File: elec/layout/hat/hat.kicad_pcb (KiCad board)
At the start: 4 copper layers, 72 parts

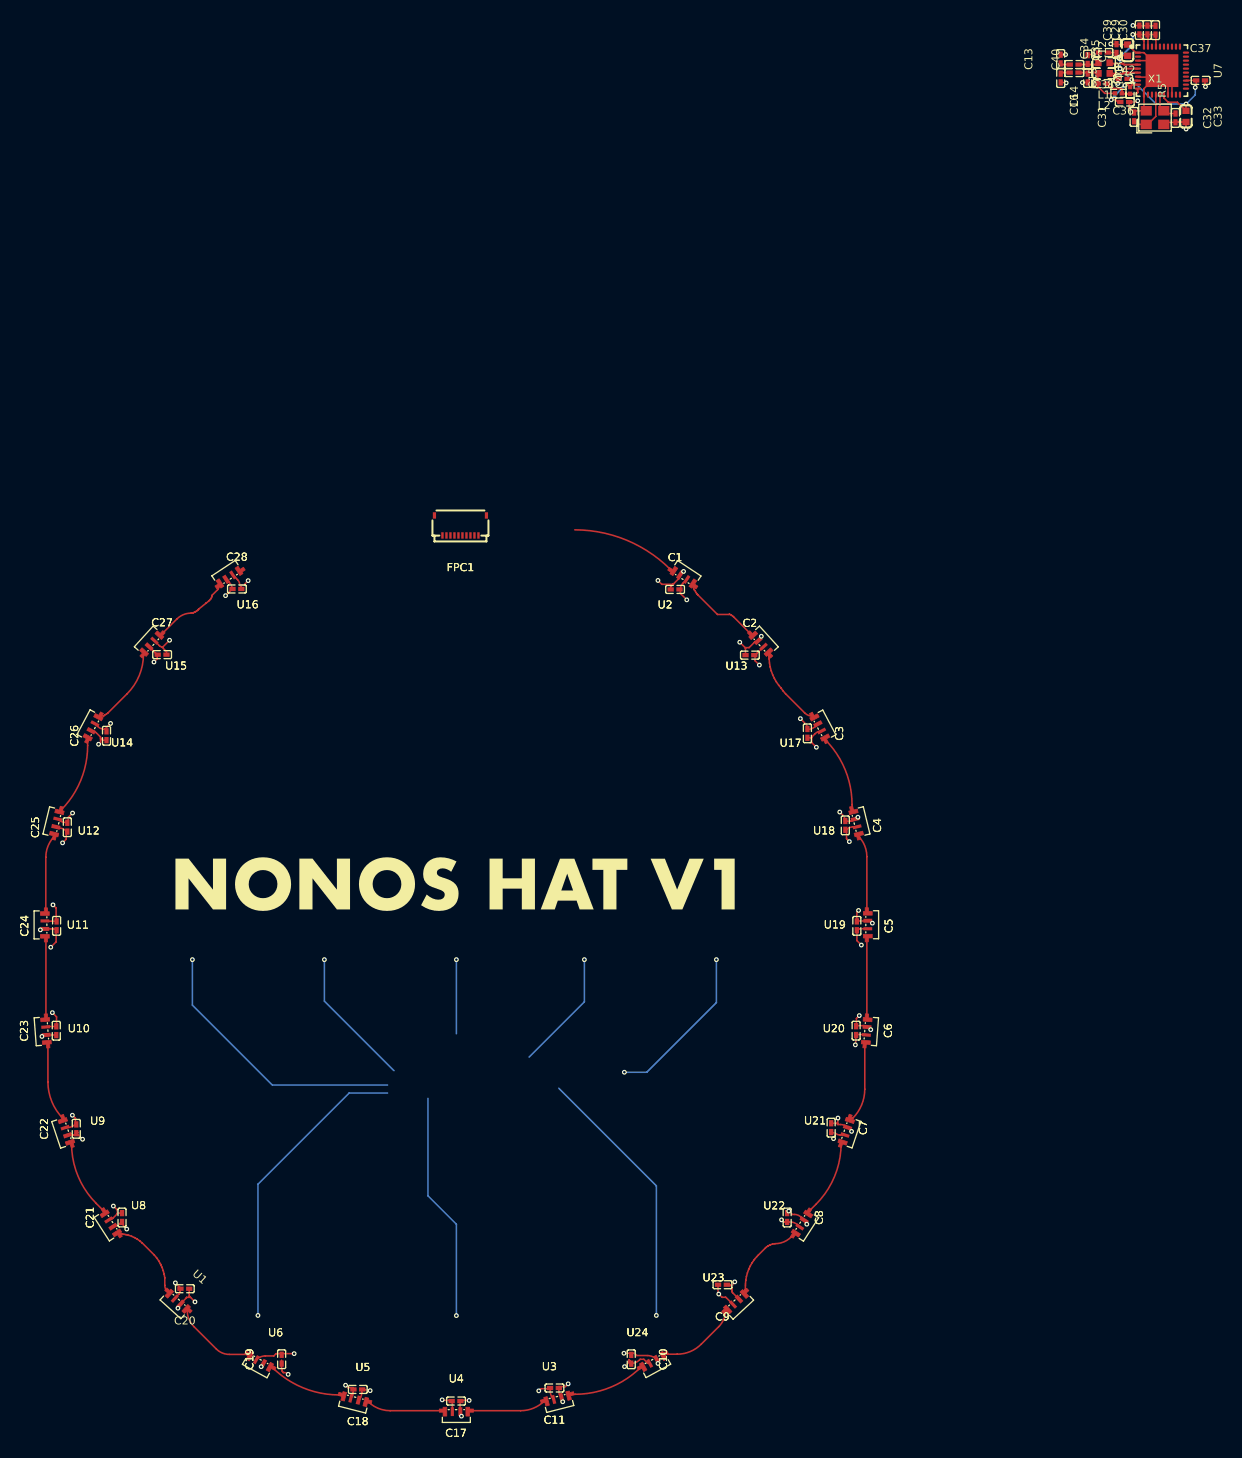
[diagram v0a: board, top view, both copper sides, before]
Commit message: layout updates, level shifter
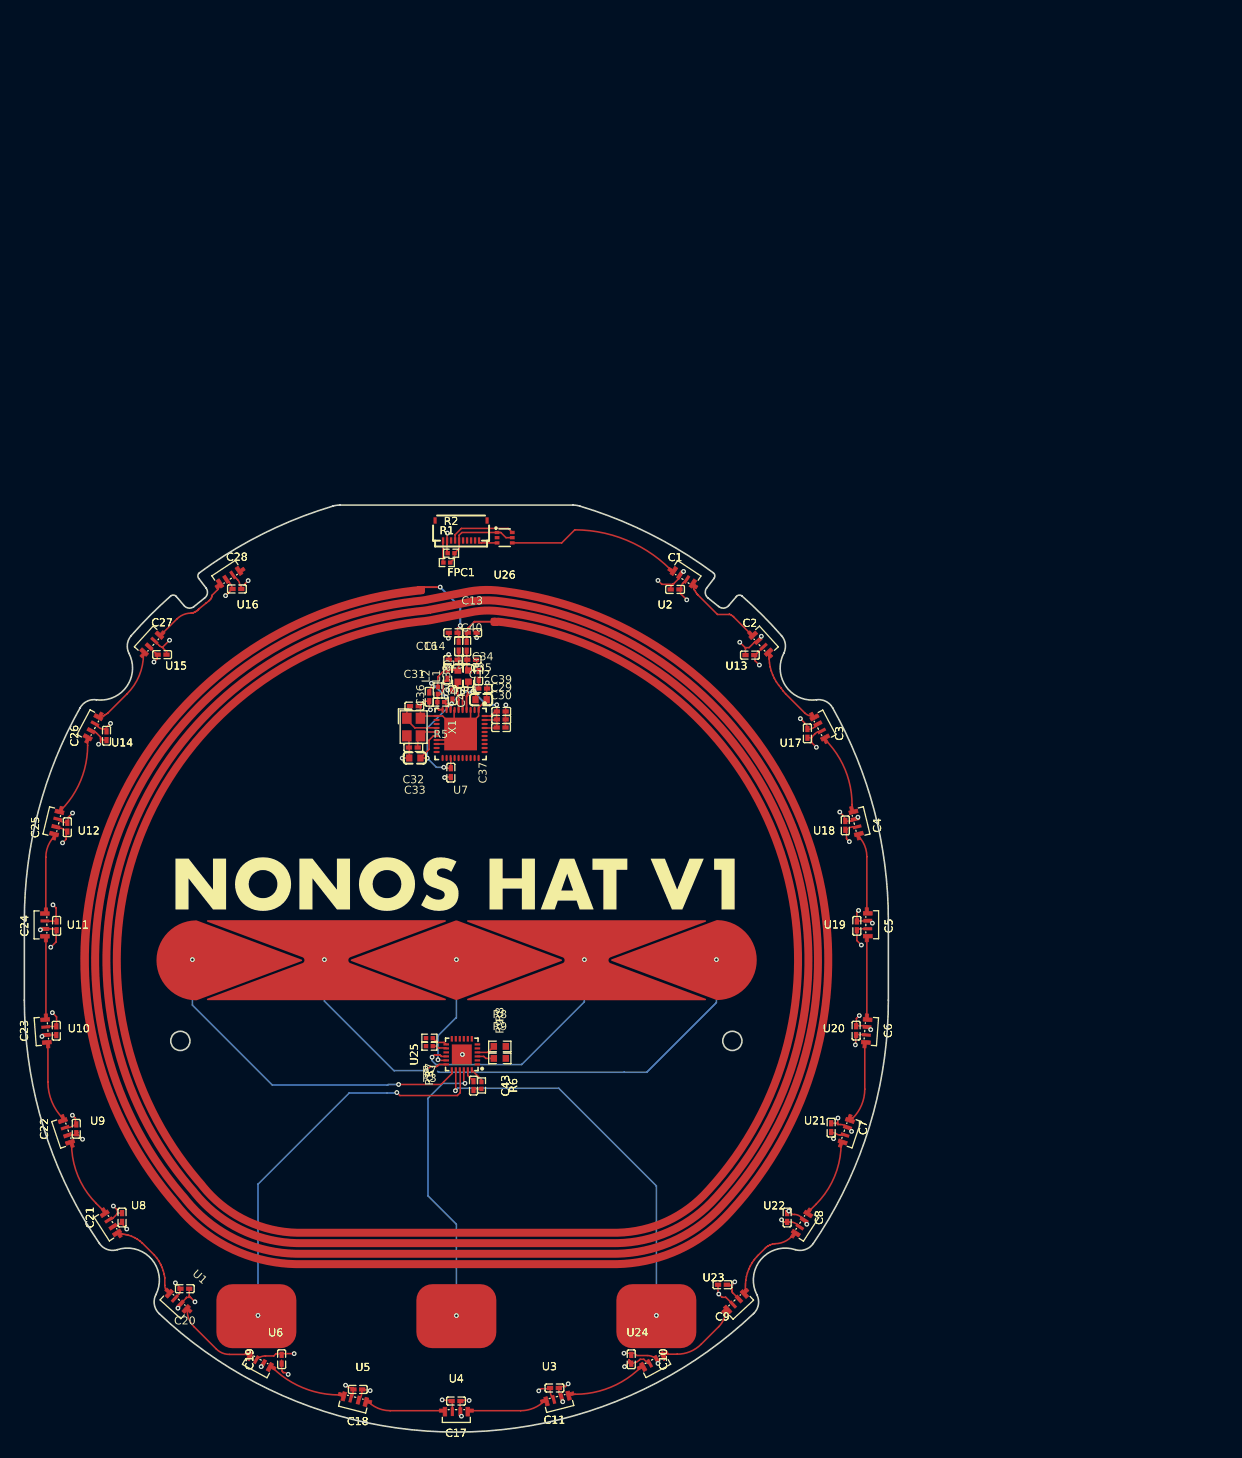
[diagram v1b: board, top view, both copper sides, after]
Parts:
- added ANT1: , hat-button-antenna:hat-button-antenna, F.Cu at (151.8, 91.2)
- added C43: 100nF ±10% 16V X7R, Samsung_Electro_Mechanics_CL05B104KO5NNNC:C0402, F.Cu at (153.9, 106.9)
- added R1: 10kΩ ±1% 62.5mW, UNI_ROYAL_0402WGF1002TCE:R0402, F.Cu at (150.6, 41.5)
- added R2: 10kΩ ±1% 62.5mW, UNI_ROYAL_0402WGF1002TCE:R0402, F.Cu at (151.1, 40.3)
- added R3: 10kΩ ±1% 62.5mW, UNI_ROYAL_0402WGF1002TCE:R0402, F.Cu at (148.4, 101.9)
- added R6: 10kΩ ±1% 62.5mW, UNI_ROYAL_0402WGF1002TCE:R0402, F.Cu at (154.9, 106.9)
- added R7: 10kΩ ±1% 62.5mW, UNI_ROYAL_0402WGF1002TCE:R0402, F.Cu at (148.4, 100.9)
- added R8: 10kΩ ±1% 100mW, UNI_ROYAL_0603WAF1002T5E:R0603, F.Cu at (157.2, 102.0)
- added R9: 10kΩ ±1% 100mW, UNI_ROYAL_0603WAF1002T5E:R0603, F.Cu at (157.2, 103.5)
- added U25: , Microchip_Tech_CAP1188_1_CP_TR:QFN-24_L4.0-W4.0-P0.50-BL-EP2.5, F.Cu at (152.5, 103.0)
- added U26: , Diodes_Incorporated_74LVC1T45DW_7:SC-70-6_L2.2-W1.3-P0.65-LS2.1-BR, F.Cu at (157.8, 38.4)
- moved C37 127.6 mm to (151.1, 67.8), turned to -90 degrees
- moved C33 125.4 mm to (146.6, 65.9), turned to 180 degrees
- moved C32 123.6 mm to (146.4, 64.6), turned to 180 degrees
- moved U7 120.7 mm to (152.3, 62.9), turned to 180 degrees
- moved X1 120.0 mm to (146.5, 62.0), turned to -90 degrees
- moved C30 119.5 mm to (157.4, 62.1), turned to 0 degrees
- moved C29 118.1 mm to (157.4, 61.1), turned to 0 degrees
- moved C39 116.7 mm to (157.4, 60.1), turned to 0 degrees
- moved C31 116.3 mm to (146.6, 59.4), turned to 0 degrees
- moved R5 115.2 mm to (149.9, 58.9), turned to 180 degrees
- moved C35 114.6 mm to (154.9, 58.6), turned to 0 degrees
- moved C42 114.4 mm to (148.4, 58.3), turned to -90 degrees
- moved C36 113.9 mm to (151.3, 58.1), turned to 90 degrees
- moved R4 113.2 mm to (149.5, 57.5), turned to -90 degrees
- moved C34 112.6 mm to (155.1, 57.2), turned to 0 degrees
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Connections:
- C1 pad 1: leds[0]-hv -> hv
- C1 pad 2: leds[0]-gnd -> gnd
- C10 pad 1: leds[9]-hv -> hv
- C10 pad 2: leds[9]-gnd -> gnd
- C11 pad 1: leds[10]-hv -> hv
- C11 pad 2: leds[10]-gnd -> gnd
- C17 pad 1: leds[11]-hv -> hv
- C17 pad 2: leds[11]-gnd -> gnd
- C18 pad 1: leds[12]-hv -> hv
- C18 pad 2: leds[12]-gnd -> gnd
- C19 pad 1: leds[13]-hv -> hv
- C19 pad 2: leds[13]-gnd -> gnd
- C2 pad 1: leds[1]-hv -> hv
- C2 pad 2: leds[1]-gnd -> gnd
- C20 pad 1: leds[14]-hv -> hv
- C20 pad 2: leds[14]-gnd -> gnd
- C21 pad 1: leds[15]-hv -> hv
- C21 pad 2: leds[15]-gnd -> gnd
- C22 pad 1: leds[16]-hv -> hv
- C22 pad 2: leds[16]-gnd -> gnd
- C23 pad 1: leds[17]-hv -> hv
- C23 pad 2: leds[17]-gnd -> gnd
- C24 pad 1: leds[18]-hv -> hv
- C24 pad 2: leds[18]-gnd -> gnd
- C25 pad 1: leds[19]-hv -> hv
- C25 pad 2: leds[19]-gnd -> gnd
- C26 pad 1: leds[20]-hv -> hv
- C26 pad 2: leds[20]-gnd -> gnd
- C27 pad 1: leds[21]-hv -> hv
- C27 pad 2: leds[21]-gnd -> gnd
- C28 pad 1: leds[22]-hv -> hv
- C28 pad 2: leds[22]-gnd -> gnd
- C29 pad 1: hv -> hv-1
- C3 pad 1: leds[2]-hv -> hv
- C3 pad 2: leds[2]-gnd -> gnd
- C30 pad 1: hv -> hv-1
- C33 pad 1: hv -> hv-1
- C34 pad 1: hv -> hv-1
- C35 pad 1: hv -> hv-1
- C36 pad 1: hv -> hv-1
- C37 pad 1: hv -> hv-1
- C38 pad 1: hv -> hv-1
- C39 pad 1: hv -> hv-1
- C4 pad 1: leds[3]-hv -> hv
- C4 pad 2: leds[3]-gnd -> gnd
- C5 pad 1: leds[4]-hv -> hv
- C5 pad 2: leds[4]-gnd -> gnd
- C6 pad 1: leds[5]-hv -> hv
- C6 pad 2: leds[5]-gnd -> gnd
- C7 pad 1: leds[6]-hv -> hv
- C7 pad 2: leds[6]-gnd -> gnd
- C8 pad 1: leds[7]-hv -> hv
- C8 pad 2: leds[7]-gnd -> gnd
- C9 pad 1: leds[8]-hv -> hv
- C9 pad 2: leds[8]-gnd -> gnd
- FPC1 pad 1: _1 -> NSS_P50_SCL_HSU_RX
- FPC1 pad 10: _10 -> A
- FPC1 pad 2: _2 -> MOSI_SDA_HSU_TX
- FPC1 pad 3: _3 -> hv
- FPC1 pad 4: _4 -> gnd
- FPC1 pad 5: _5 -> hv-1
- FPC1 pad 6: _6 -> gnd
- FPC1 pad 7: _7 -> RSTOUT_N
- FPC1 pad 8: _8 -> P70_IRQ
- FPC1 pad 9: _9 -> nALERT_nBC_IRQ
- U1 pad 1: leds[14]-DOUT -> DOUT-5
- U1 pad 2: leds[14]-gnd -> gnd
- U1 pad 3: leds[14]-hv -> hv
- U1 pad 4: leds[14]-DIN -> DOUT-4
- U10 pad 1: leds[17]-DOUT -> DOUT-8
- U10 pad 2: leds[17]-gnd -> gnd
- U10 pad 3: leds[17]-hv -> hv
- U10 pad 4: leds[17]-DIN -> DOUT-7
- U11 pad 1: leds[18]-DOUT -> DOUT-9
- U11 pad 2: leds[18]-gnd -> gnd
- U11 pad 3: leds[18]-hv -> hv
- U11 pad 4: leds[18]-DIN -> DOUT-8
- U12 pad 1: leds[19]-DOUT -> DOUT-10
- U12 pad 2: leds[19]-gnd -> gnd
- U12 pad 3: leds[19]-hv -> hv
- U12 pad 4: leds[19]-DIN -> DOUT-9
- U13 pad 1: leds[1]-DOUT -> DOUT-11
- U13 pad 2: leds[1]-gnd -> gnd
- U13 pad 3: leds[1]-hv -> hv
- U13 pad 4: leds[1]-DIN -> DOUT
- U14 pad 1: leds[20]-DOUT -> DOUT-12
- U14 pad 2: leds[20]-gnd -> gnd
- U14 pad 3: leds[20]-hv -> hv
- U14 pad 4: leds[20]-DIN -> DOUT-10
- U15 pad 1: leds[21]-DOUT -> DOUT-13
- U15 pad 2: leds[21]-gnd -> gnd
- U15 pad 3: leds[21]-hv -> hv
- U15 pad 4: leds[21]-DIN -> DOUT-12
- U16 pad 2: leds[22]-gnd -> gnd
- U16 pad 3: leds[22]-hv -> hv
- U16 pad 4: leds[22]-DIN -> DOUT-13
- U17 pad 1: leds[2]-DOUT -> DOUT-14
- U17 pad 2: leds[2]-gnd -> gnd
- U17 pad 3: leds[2]-hv -> hv
- U17 pad 4: leds[2]-DIN -> DOUT-11
- U18 pad 1: leds[3]-DOUT -> DOUT-15
- U18 pad 2: leds[3]-gnd -> gnd
- U18 pad 3: leds[3]-hv -> hv
- U18 pad 4: leds[3]-DIN -> DOUT-14
- U19 pad 1: leds[4]-DOUT -> DOUT-16
- U19 pad 2: leds[4]-gnd -> gnd
- U19 pad 3: leds[4]-hv -> hv
- U19 pad 4: leds[4]-DIN -> DOUT-15
- U2 pad 1: leds[0]-DOUT -> DOUT
- U2 pad 2: leds[0]-gnd -> gnd
- U2 pad 3: leds[0]-hv -> hv
- U2 pad 4: leds[0]-DIN -> DIN
- U20 pad 1: leds[5]-DOUT -> DOUT-17
- U20 pad 2: leds[5]-gnd -> gnd
- U20 pad 3: leds[5]-hv -> hv
- U20 pad 4: leds[5]-DIN -> DOUT-16
- U21 pad 1: leds[6]-DOUT -> DOUT-18
- U21 pad 2: leds[6]-gnd -> gnd
- U21 pad 3: leds[6]-hv -> hv
- U21 pad 4: leds[6]-DIN -> DOUT-17
- U22 pad 1: leds[7]-DOUT -> DOUT-19
- U22 pad 2: leds[7]-gnd -> gnd
- U22 pad 3: leds[7]-hv -> hv
- U22 pad 4: leds[7]-DIN -> DOUT-18
- U23 pad 1: leds[8]-DOUT -> DOUT-20
- U23 pad 2: leds[8]-gnd -> gnd
- U23 pad 3: leds[8]-hv -> hv
- U23 pad 4: leds[8]-DIN -> DOUT-19
- U24 pad 1: leds[9]-DOUT -> DIN-1
- U24 pad 2: leds[9]-gnd -> gnd
- U24 pad 3: leds[9]-hv -> hv
- U24 pad 4: leds[9]-DIN -> DOUT-20
- U3 pad 1: leds[10]-DOUT -> DOUT-1
- U3 pad 2: leds[10]-gnd -> gnd
- U3 pad 3: leds[10]-hv -> hv
- U3 pad 4: leds[10]-DIN -> DIN-1
- U4 pad 1: leds[11]-DOUT -> DOUT-2
- U4 pad 2: leds[11]-gnd -> gnd
- U4 pad 3: leds[11]-hv -> hv
- U4 pad 4: leds[11]-DIN -> DOUT-1
- U5 pad 1: leds[12]-DOUT -> DOUT-3
- U5 pad 2: leds[12]-gnd -> gnd
- U5 pad 3: leds[12]-hv -> hv
- U5 pad 4: leds[12]-DIN -> DOUT-2
- U6 pad 1: leds[13]-DOUT -> DOUT-4
- U6 pad 2: leds[13]-gnd -> gnd
- U6 pad 3: leds[13]-hv -> hv
- U6 pad 4: leds[13]-DIN -> DOUT-3
- U7 pad 16: hv -> hv-1
- U7 pad 23: hv -> hv-1
- U7 pad 37: hv -> hv-1
- U7 pad 39: hv -> hv-1
- U7 pad 40: hv -> hv-1
- U7 pad 5: hv -> hv-1
- U7 pad 8: hv -> hv-1
- U8 pad 1: leds[15]-DOUT -> DOUT-6
- U8 pad 2: leds[15]-gnd -> gnd
- U8 pad 3: leds[15]-hv -> hv
- U8 pad 4: leds[15]-DIN -> DOUT-5
- U9 pad 1: leds[16]-DOUT -> DOUT-7
- U9 pad 2: leds[16]-gnd -> gnd
- U9 pad 3: leds[16]-hv -> hv
- U9 pad 4: leds[16]-DIN -> DOUT-6
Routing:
- net gnd: track 42.6 -> 117.6 mm, vias 10 -> 34
- net hv-1: track 0.00 -> 49.0 mm, vias 0 -> 6
- net hv: track 38.1 -> 86.6 mm, vias 6 -> 36
- net slider[4]: track 20.5 -> 43.9 mm, vias 2 -> 1
- net DIN: track 0.00 -> 21.9 mm
- net next_button: track 33.5 -> 49.1 mm, vias 1 -> 2
- net slider[3]: track 15.0 -> 30.2 mm, vias 1 -> 2
- net leds[0]-DIN: track 13.4 -> 0.00 mm
- net prev_button: track 37.5 -> 49.8 mm, vias 1 -> 2
- net leds[13]-DOUT: track 10.4 -> 0.00 mm
- net DOUT-4: track 0.00 -> 10.4 mm
- net leds[15]-DIN: track 10.4 -> 0.00 mm
- net DOUT-5: track 0.00 -> 10.4 mm
- net leds[8]-DIN: track 10.4 -> 0.00 mm
- net DOUT-19: track 0.00 -> 10.4 mm
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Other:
- board outline added: 108 x 115.9 mm

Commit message: layout complete
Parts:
- added C44: 100nF ±10% 16V X7R, Samsung_Electro_Mechanics_CL05B104KO5NNNC:C0402, F.Cu at (0.00, 0.00)
- added C45: 100nF ±10% 16V X7R, Samsung_Electro_Mechanics_CL05B104KO5NNNC:C0402, F.Cu at (0.00, -10.0)
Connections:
- C43 pad 1: VDD -> hv-1
- U25 pad 23: VDD -> hv-1
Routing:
- net hv-1: track 49.0 -> 134.4 mm, vias 6 -> 10
- net MOSI_SDA_HSU_TX: track 6.54 -> 90.9 mm, vias 1 -> 3
- net NSS_P50_SCL_HSU_RX: track 4.94 -> 88.7 mm, vias 0 -> 3
- net gnd: track 117.6 -> 196.8 mm, vias 34 -> 39
- net nALERT_nBC_IRQ: track 1.99 -> 73.6 mm, vias 0 -> 2
- net P70_IRQ: track 0.00 -> 38.1 mm, vias 0 -> 2
- net RSTOUT_N: track 0.00 -> 35.7 mm, vias 0 -> 2
- net slider[4]: track 43.9 -> 49.3 mm, vias 1 -> 2
- net VDD: track 1.69 -> 0.00 mm
- net hv: track 86.6 -> 87.2 mm, vias 36 -> 37
- added copper zone on F.Cu, net gnd
- added copper zone on In1.Cu, net gnd
- added copper zone on In2.Cu, net gnd
- added copper zone on B.Cu, net hv

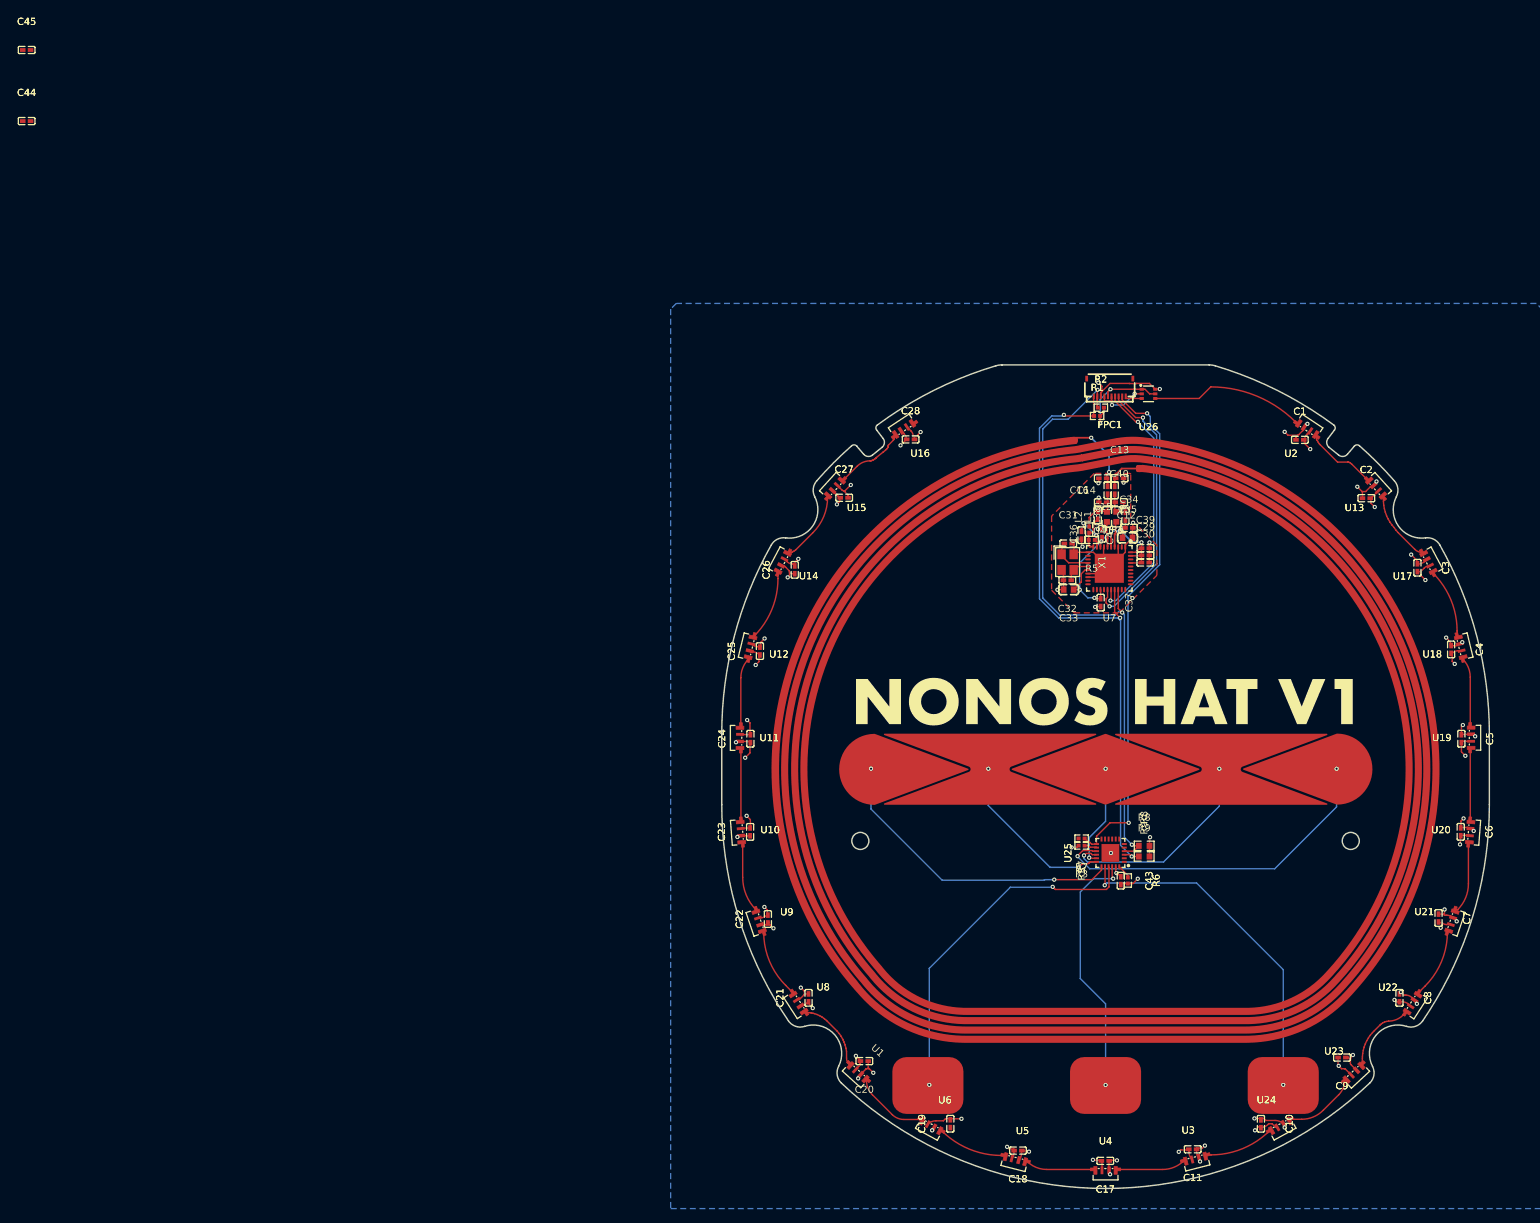
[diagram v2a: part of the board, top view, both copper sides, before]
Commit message: Cleanup silkscreen
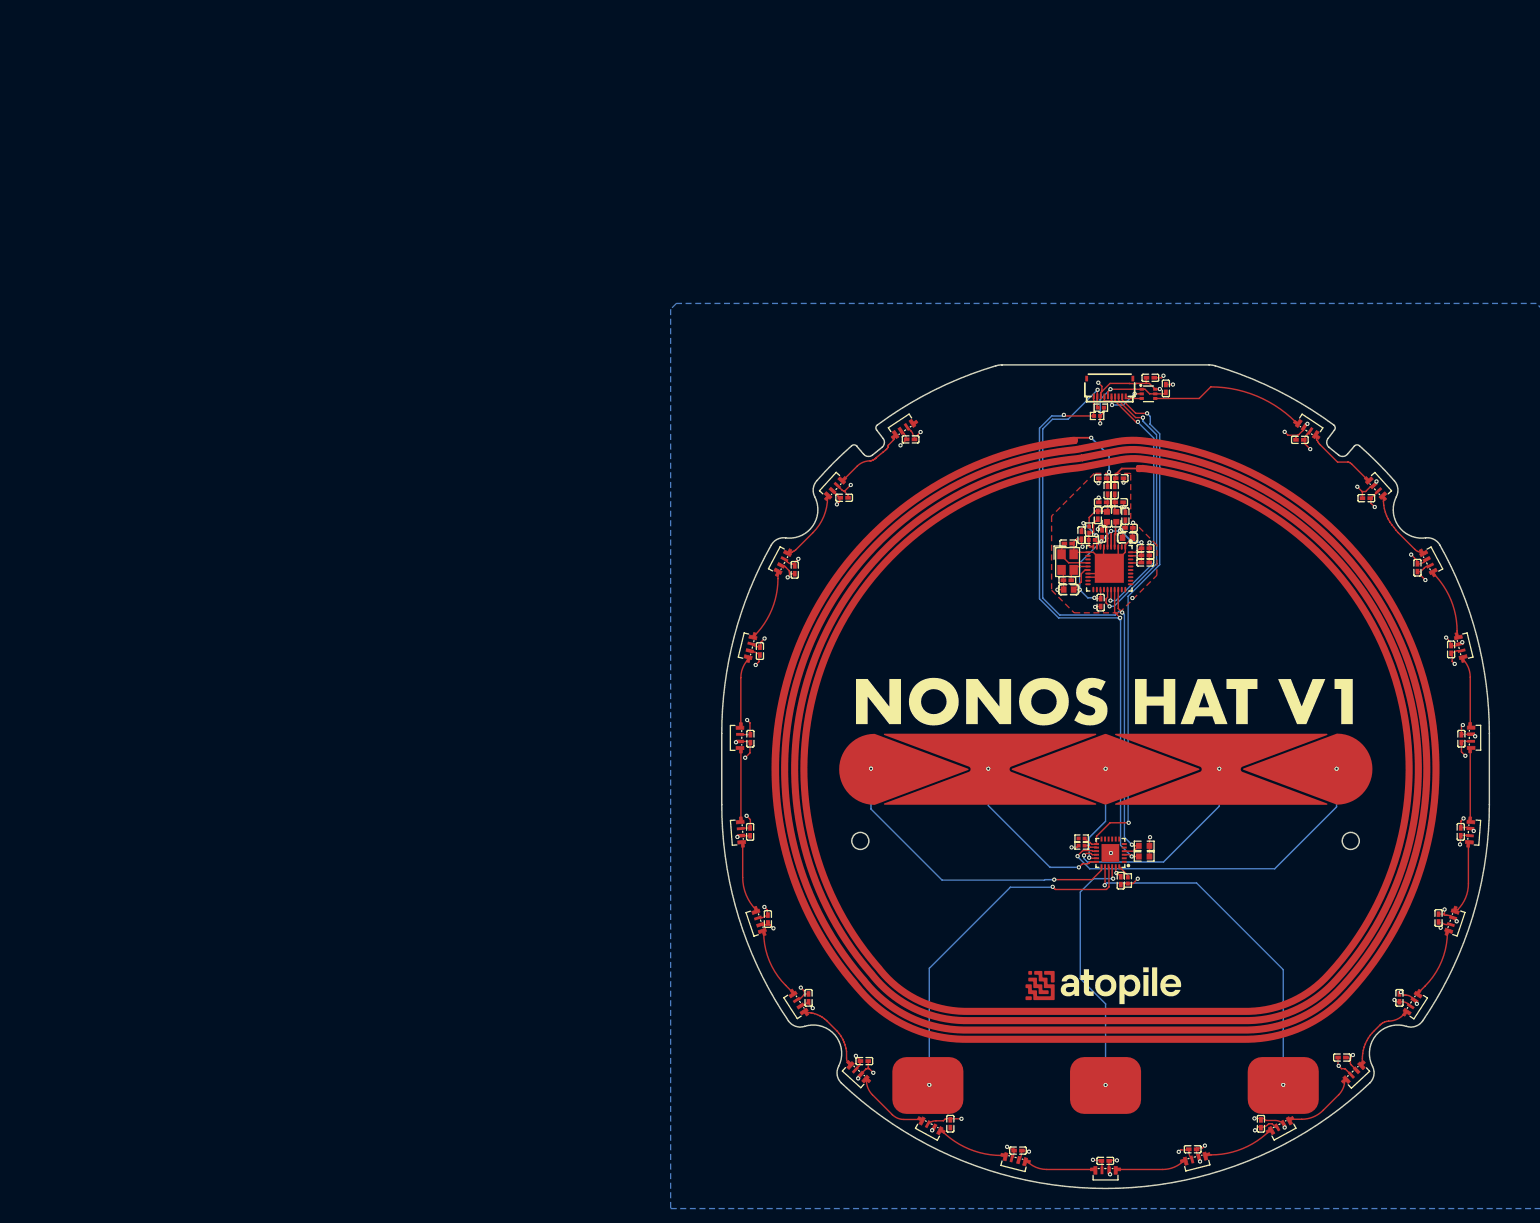
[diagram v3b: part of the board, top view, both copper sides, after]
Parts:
- moved C45 164.7 mm to (158.1, 36.1)
- moved C44 164.6 mm to (160.3, 37.6), turned to 90 degrees
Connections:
- C44 pad 1: level_shifter.caps[0]-net -> hv-1
- C44 pad 2: level_shifter.caps[0]-net-1 -> gnd
- C45 pad 1: level_shifter.caps[1]-net -> hv
- C45 pad 2: level_shifter.caps[1]-net-1 -> gnd
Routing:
- net gnd: track 196.8 -> 199.2 mm, vias 39 -> 41
- net hv-1: track 134.4 -> 136.0 mm
- net hv: track 87.2 -> 88.1 mm
